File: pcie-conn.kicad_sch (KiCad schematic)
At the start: 22 parts, among them J2 Bus_M.2_1-2199230-6

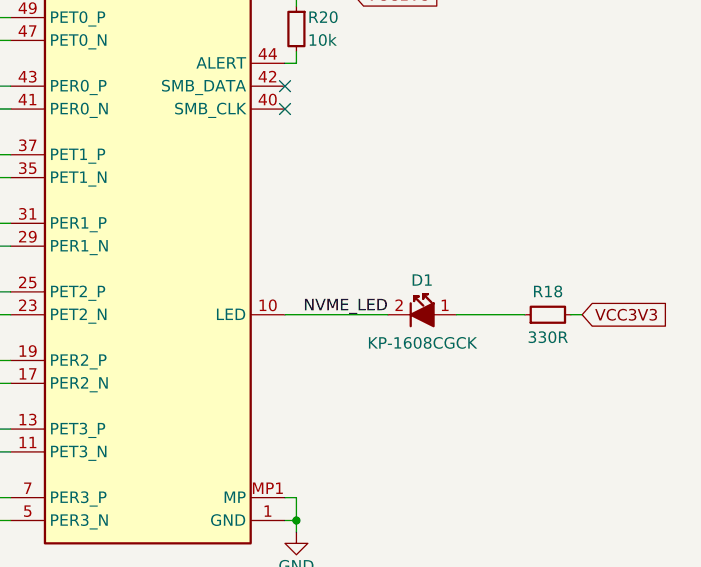
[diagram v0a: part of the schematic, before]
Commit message: [#68236] Update symbols and footprints, clean ERC and DRC
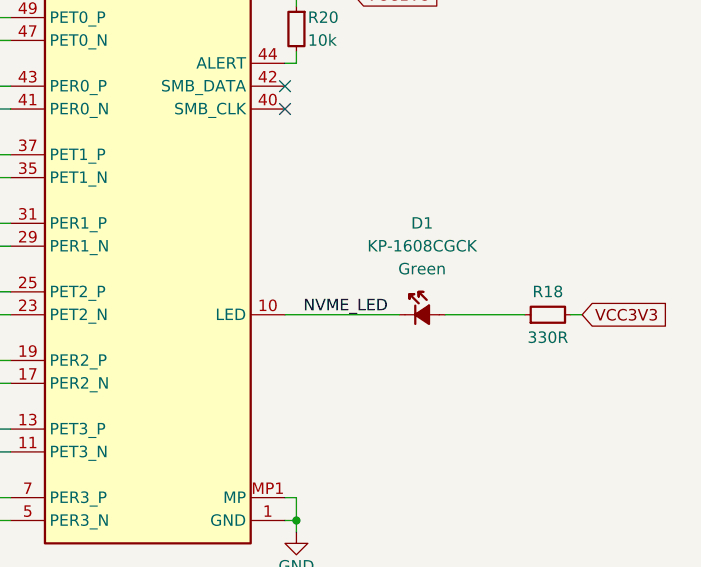
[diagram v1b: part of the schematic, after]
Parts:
- C179, C180, C181, C182, C27, C28, C29, C30: Public (none) -> False
- D1: Color (none) -> Green
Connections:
- net NVME_LED: now also D1.1 (C); no longer D1.2
- net at R18.1: now also D1.2 (A); no longer D1.1
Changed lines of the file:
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@@
     (stroke (width 0) (type default))
   )
-  (wire (pts (xy 264.16 152.4) (xy 271.78 152.4))
+  (wire (pts (xy 262.89 152.4) (xy 271.78 152.4))
     (stroke (width 0) (type default))
   )
@@
     (stroke (width 0) (type default))
   )
-  (wire (pts (xy 245.11 152.4) (xy 256.54 152.4))
+  (wire (pts (xy 245.11 152.4) (xy 257.81 152.4))
     (stroke (width 0) (type default))
   )
@@
       (effects (font (size 1.27 1.27)) (justify left bottom) hide)
     )
+    (property "Public" "False" (at 166.37 86.36 0)
+      (effects (font (size 1.27 1.27)) (justify left bottom) hide)
+    )
     (pin "1")
     (pin "2")
@@
       (effects (font (size 1.27 1.27)) (justify left bottom) hide)
     )
+    (property "Public" "False" (at 163.83 88.9 0)
+      (effects (font (size 1.27 1.27)) (justify left bottom) hide)
+    )
     (pin "1")
     (pin "2")
@@
       (effects (font (size 1.27 1.27)) (justify left bottom) hide)
     )
+    (property "Public" "False" (at 166.37 101.6 0)
+      (effects (font (size 1.27 1.27)) (justify left bottom) hide)
+    )
     (pin "1")
     (pin "2")
@@
     )
     (property "Dielectric" "" (at 163.83 106.68 0)
+      (effects (font (size 1.27 1.27)) (justify left bottom) hide)
+    )
+    (property "Public" "False" (at 163.83 104.14 0)
       (effects (font (size 1.27 1.27)) (justify left bottom) hide)
     )
@@
     )
   )
-  (symbol (lib_id "antmicroLEDIndicationDiscrete:LED_G_0603_KP-1608CGCK") (at 264.16 152.4 0) (mirror y) (unit 1)
-    (in_bom yes) (on_board yes) (dnp no)
-    (property "Reference" "D1" (at 260.35 148.59 0)
-      (effects (font (size 1.27 1.27)))
-    )
-    (property "Value" "LED_G_0603_KP-1608CGCK" (at 241.3 160.02 0)
-      (effects (font (size 1.27 1.27) (thickness 0.15)) (justify left bottom) hide)
-    )
-    (property "Footprint" "antmicro-footprints:LED_0603_1608Metric_G" (at 241.3 162.56 0)
-      (effects (font (size 1.27 1.27) (thickness 0.15)) (justify left bottom) hide)
-    )
-    (property "Datasheet" "http://www.farnell.com/datasheets/2045956.pdf" (at 241.3 165.1 0)
-      (effects (font (size 1.27 1.27) (thickness 0.15)) (justify left bottom) hide)
-    )
-    (property "MPN" "KP-1608CGCK" (at 260.35 155.575 0)
-      (effects (font (size 1.27 1.27) (thickness 0.15)))
-    )
-    (property "Manufacturer" "Kingbright" (at 241.3 170.18 0)
-      (effects (font (size 1.27 1.27) (thickness 0.15)) (justify left bottom) hide)
-    )
-    (property "Author" "Antmicro" (at 241.3 172.72 0)
-      (effects (font (size 1.27 1.27) (thickness 0.15)) (justify left bottom) hide)
-    )
-    (property "License" "Apache-2.0" (at 241.3 175.26 0)
-      (effects (font (size 1.27 1.27) (thickness 0.15)) (justify left bottom) hide)
-    )
-    (pin "1")
-    (pin "2")
-    (instances
-      (project "artix-dc-scm"
-        (path "/f3cd042e-9a46-4397-9768-c62eb1c291be/00000000-0000-0000-0000-00005fd17ef1"
-          (reference "D1") (unit 1)
-        )
-      )
-    )
-  )
   (symbol (lib_id "antmicroResistors0402:R_330R_0402") (at 271.78 152.4 0) (mirror x) (unit 1)
     (in_bom yes) (on_board yes) (dnp no)
@@
       (effects (font (size 1.27 1.27)) (justify left bottom) hide)
     )
+    (property "Public" "False" (at 166.37 116.84 0)
+      (effects (font (size 1.27 1.27)) (justify left bottom) hide)
+    )
     (pin "1")
     (pin "2")
@@
       (effects (font (size 1.27 1.27)) (justify left bottom) hide)
     )
+    (property "Public" "False" (at 163.83 119.38 0)
+      (effects (font (size 1.27 1.27)) (justify left bottom) hide)
+    )
     (pin "1")
     (pin "2")
@@
       (effects (font (size 1.27 1.27)) (justify left bottom) hide)
     )
+    (property "Public" "False" (at 166.37 132.08 0)
+      (effects (font (size 1.27 1.27)) (justify left bottom) hide)
+    )
     (pin "1")
     (pin "2")
@@
     )
     (property "Dielectric" "" (at 163.83 137.16 0)
+      (effects (font (size 1.27 1.27)) (justify left bottom) hide)
+    )
+    (property "Public" "False" (at 163.83 134.62 0)
       (effects (font (size 1.27 1.27)) (justify left bottom) hide)
     )
@@
         )
       )
+    )
+  )
+  (symbol (lib_id "antmicroLEDIndicationDiscrete:LED_G_0603_KP-1608CGCK") (at 257.81 152.4 0) (unit 1)
+    (in_bom yes) (on_board yes) (dnp no) (fields_autoplaced)
+    (property "Reference" "D1" (at 260.35 142.24 0)
+      (effects (font (size 1.27 1.27)))
+    )
+    (property "Value" "LED_G_0603_KP-1608CGCK" (at 280.67 160.02 0)
+      (effects (font (size 1.27 1.27) (thickness 0.15)) (justify left bottom) hide)
+    )
+    (property "Footprint" "antmicro-footprints:LED_0603_1608Metric_G" (at 280.67 162.56 0)
+      (effects (font (size 1.27 1.27) (thickness 0.15)) (justify left bottom) hide)
+    )
+    (property "Datasheet" "http://www.kingbright.com/attachments/file/psearch//000/00/00/KP-1608CGCK(Ver.23B).pdf" (at 280.67 165.1 0)
+      (effects (font (size 1.27 1.27) (thickness 0.15)) (justify left bottom) hide)
+    )
+    (property "MPN" "KP-1608CGCK" (at 260.35 144.78 0)
+      (effects (font (size 1.27 1.27) (thickness 0.15)))
+    )
+    (property "Manufacturer" "Kingbright" (at 280.67 170.18 0)
+      (effects (font (size 1.27 1.27) (thickness 0.15)) (justify left bottom) hide)
+    )
+    (property "Author" "Antmicro" (at 280.67 172.72 0)
+      (effects (font (size 1.27 1.27) (thickness 0.15)) (justify left bottom) hide)
+    )
+    (property "License" "Apache-2.0" (at 280.67 175.26 0)
+      (effects (font (size 1.27 1.27) (thickness 0.15)) (justify left bottom) hide)
+    )
+    (property "Color" "Green" (at 260.35 147.32 0)
+      (effects (font (size 1.27 1.27)))
+    )
+    (pin "1")
+    (pin "2")
+    (instances
+      (project "artix-dc-scm"
+        (path "/f3cd042e-9a46-4397-9768-c62eb1c291be/00000000-0000-0000-0000-00005fd17ef1"
+          (reference "D1") (unit 1)
+        )
+      )

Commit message: a lot of routing and almost all caps of the fpga are placed down
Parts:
- C179, C180, C181, C182, C27, C28, C29, C30, C31, C32, C33, C34: footprint antmicro-footprints:C_0402_1005Metric -> Capacitor_SMD:C_0402_1005Metric
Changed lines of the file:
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@@
 			)
 		)
-		(property "Footprint" "antmicro-footprints:C_0402_1005Metric"
+		(property "Footprint" "Capacitor_SMD:C_0402_1005Metric"
 			(at 166.37 106.68 0)
 			(hide yes)
@@
 			)
 		)
-		(property "Footprint" "antmicro-footprints:C_0402_1005Metric"
+		(property "Footprint" "Capacitor_SMD:C_0402_1005Metric"
 			(at 163.83 109.22 0)
 			(hide yes)
@@
 			)
 		)
-		(property "Footprint" "antmicro-footprints:C_0402_1005Metric"
+		(property "Footprint" "Capacitor_SMD:C_0402_1005Metric"
 			(at 166.37 121.92 0)
 			(hide yes)
@@
 			)
 		)
-		(property "Footprint" "antmicro-footprints:C_0402_1005Metric"
+		(property "Footprint" "Capacitor_SMD:C_0402_1005Metric"
 			(at 163.83 124.46 0)
 			(hide yes)
@@
 			)
 		)
-		(property "Footprint" "antmicro-footprints:C_0402_1005Metric"
+		(property "Footprint" "Capacitor_SMD:C_0402_1005Metric"
 			(at 259.08 83.82 0)
 			(hide yes)
@@
 			)
 		)
-		(property "Footprint" "antmicro-footprints:C_0402_1005Metric"
+		(property "Footprint" "Capacitor_SMD:C_0402_1005Metric"
 			(at 266.7 83.82 0)
 			(hide yes)
@@
 			)
 		)
-		(property "Footprint" "antmicro-footprints:C_0402_1005Metric"
+		(property "Footprint" "Capacitor_SMD:C_0402_1005Metric"
 			(at 274.32 83.82 0)
 			(hide yes)
@@
 			)
 		)
-		(property "Footprint" "antmicro-footprints:C_0402_1005Metric"
+		(property "Footprint" "Capacitor_SMD:C_0402_1005Metric"
 			(at 281.94 83.82 0)
 			(hide yes)
@@
 			)
 		)
-		(property "Footprint" "antmicro-footprints:C_0402_1005Metric"
+		(property "Footprint" "Capacitor_SMD:C_0402_1005Metric"
 			(at 166.37 137.16 0)
 			(hide yes)
@@
 			)
 		)
-		(property "Footprint" "antmicro-footprints:C_0402_1005Metric"
+		(property "Footprint" "Capacitor_SMD:C_0402_1005Metric"
 			(at 163.83 139.7 0)
 			(hide yes)
@@
 			)
 		)
-		(property "Footprint" "antmicro-footprints:C_0402_1005Metric"
+		(property "Footprint" "Capacitor_SMD:C_0402_1005Metric"
 			(at 166.37 152.4 0)
 			(hide yes)
@@
 			)
 		)
-		(property "Footprint" "antmicro-footprints:C_0402_1005Metric"
+		(property "Footprint" "Capacitor_SMD:C_0402_1005Metric"
 			(at 163.83 154.94 0)
 			(hide yes)

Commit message: version 1.0 complete
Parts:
- D1: MPN KP-1608CGCK -> SML-D13FWT86C; Manufacturer Kingbright -> ROHM Semiconductor
- R17, R19, R20: MPN CR0402-FX-1002GLF -> CR0402AFX-1002GAS

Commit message: "In the process of upgrading the ddr memory"
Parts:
- removed H1: Spacer_Drill3.7mm_H2.5mm_9774025151R, antmicro-footprints:Spacer_Drill3.7mm_H2.5mm_9774025151R, symbol antmicroMechanicalParts:Spacer_Drill3.7mm_H2.5mm_9774025151R
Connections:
- no-connect marks 4 -> 3
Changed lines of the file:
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@@
 	)
 	(no_connect
-		(at 224.79 185.42)
-	)
-	(no_connect
 		(at 245.11 110.49)
 	)
@@
 				)
 			)
-		)
-	)
-	(symbol
-		(lib_id "antmicroMechanicalParts:Spacer_Drill3.7mm_H2.5mm_9774025151R")
-		(at 224.79 185.42 0)
-		(unit 1)
-		(body_style 1)
-		(exclude_from_sim no)
-		(in_bom yes)
-		(on_board yes)
-		(in_pos_files yes)
-		(dnp no)
-		(fields_autoplaced yes)
-		(property "Reference" "H1"
-			(at 233.68 184.15 0)
-			(show_name no)
-			(do_not_autoplace no)
-			(effects
-				(font
-					(size 1.27 1.27)
-					(thickness 0.15)
-				)
-				(justify left)
-			)
-		)
-		(property "Value" "Spacer_Drill3.7mm_H2.5mm_9774025151R"
-			(at 233.68 186.69 0)
-			(show_name no)
-			(do_not_autoplace no)
-			(effects
-				(font
-					(size 1.27 1.27)
-					(thickness 0.15)
-				)
-				(justify left)
-			)
-		)
-		(property "Footprint" "antmicro-footprints:Spacer_Drill3.7mm_H2.5mm_9774025151R"
-			(at 247.65 193.04 0)
-			(hide yes)
-			(show_name no)
-			(do_not_autoplace no)
-			(effects
-				(font
-					(size 1.27 1.27)
-					(thickness 0.15)
-				)
-				(justify left bottom)
-			)
-		)
-		(property "Datasheet" "https://www.we-online.com/components/products/datasheet/9774025151R.pdf"
-			(at 247.65 195.58 0)
-			(hide yes)
-			(show_name no)
-			(do_not_autoplace no)
-			(effects
-				(font
-					(size 1.27 1.27)
-					(thickness 0.15)
-				)
-				(justify left bottom)
-			)
-		)
-		(property "Description" "Spacer, SMT, Non Stop, Steel, Swage Round, 5.1 mm x 2.5 mm, M2.5 Thread, WA-SMSI Series"
-			(at 224.79 185.42 0)
-			(hide yes)
-			(show_name no)
-			(do_not_autoplace no)
-			(effects
-				(font
-					(size 1.27 1.27)
-				)
-			)
-		)
-		(property "Manufacturer" "Würth Elektronik"
-			(at 247.65 198.12 0)
-			(hide yes)
-			(show_name no)
-			(do_not_autoplace no)
-			(effects
-				(font
-					(size 1.27 1.27)
-					(thickness 0.15)
-				)
-				(justify left bottom)
-			)
-		)
-		(property "MPN" "9774025151R"
-			(at 247.65 200.66 0)
-			(hide yes)
-			(show_name no)
-			(do_not_autoplace no)
-			(effects
-				(font
-					(size 1.27 1.27)
-					(thickness 0.15)
-				)
-				(justify left bottom)
-			)
-		)
-		(property "Author" "Antmicro"
-			(at 247.65 203.2 0)
-			(hide yes)
-			(show_name no)
-			(do_not_autoplace no)
-			(effects
-				(font
-					(size 1.27 1.27)
-					(thickness 0.15)
-				)
-				(justify left bottom)
-			)
-		)
-		(property "License" "Apache-2.0"
-			(at 247.65 205.74 0)
-			(hide yes)
-			(show_name no)
-			(do_not_autoplace no)
-			(effects
-				(font
-					(size 1.27 1.27)
-					(thickness 0.15)
-				)
-				(justify left bottom)
-			)
-		)
-		(pin "1"
-		)
-		(instances
-			(project "artix-dc-scm"
-				(path "/f3cd042e-9a46-4397-9768-c62eb1c291be/00000000-0000-0000-0000-00005fd17ef1"
-					(reference "H1")
-					(unit 1)
-					(variant
-						(name "resistor")
-					)
-				)
-			)
